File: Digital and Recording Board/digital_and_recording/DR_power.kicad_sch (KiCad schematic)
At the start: 2 parts

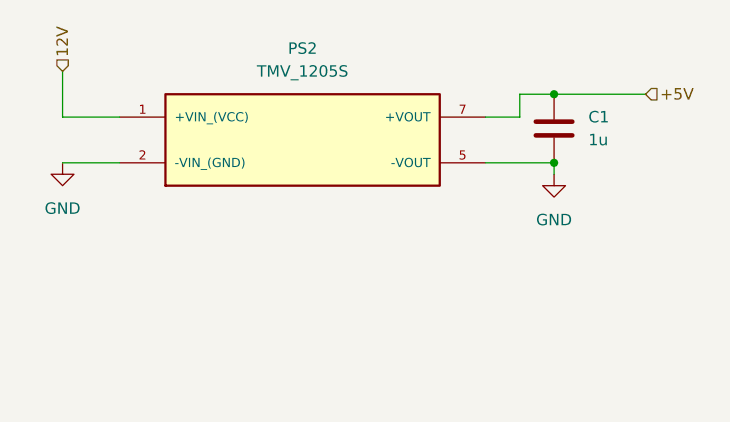
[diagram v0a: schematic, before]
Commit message: updated schematic to use +/-5 DCDC
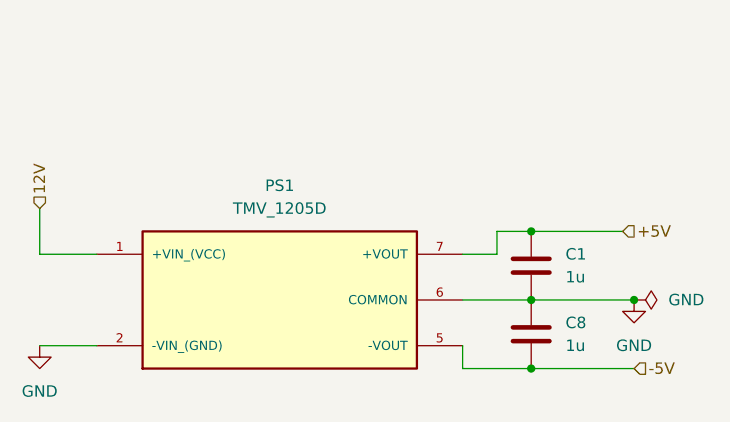
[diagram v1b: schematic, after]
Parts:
- removed PS2: TMV_1205S, TMV_1205S:CONV_TMV_1205S, symbol TMV_1205S:TMV_1205S
- added C8: 1u, Capacitor_SMD:C_0201_0603Metric, symbol Device:C
- added PS1: TMV_1205D, TMV_1205D:CONV_TMV_1205D, symbol TMV_1205D:TMV_1205D
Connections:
- net +5V: now also PS1.7 (+VOUT)
- net 12V: now also PS1.1 (+VIN_(VCC))
- net GND: now also C8.1, PS1.2 (-VIN_(GND)), PS1.6 (COMMON)
- new net -5V: C8.2, PS1.5 (-VOUT)
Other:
- moved on the sheet: C1
